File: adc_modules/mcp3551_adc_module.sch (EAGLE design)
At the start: 10 parts, among them U1 MCP3553-E/SN

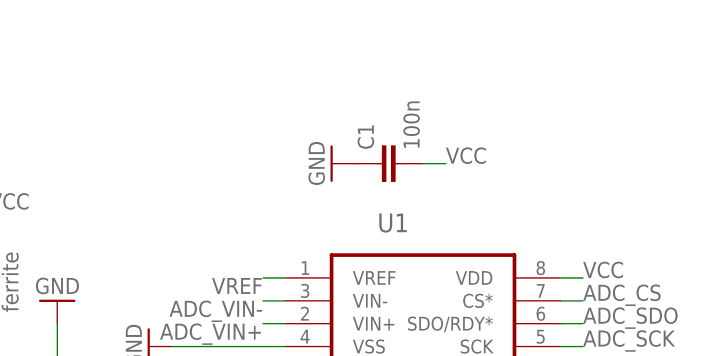
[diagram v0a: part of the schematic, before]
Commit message: * updated board format * made the LTC6655 reference module more compact, hopefully better * small modifications to the MCP355X ADC module
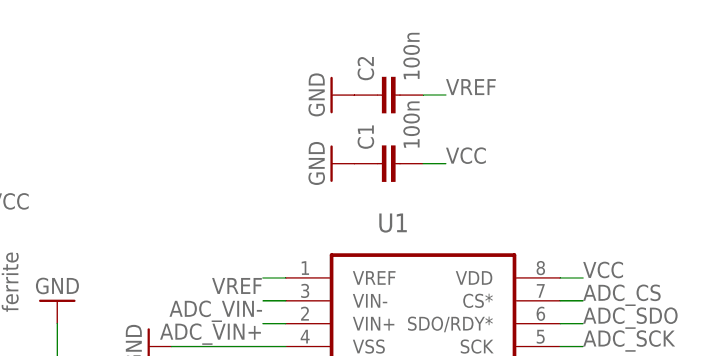
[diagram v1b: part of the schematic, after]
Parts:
- added C2: 100n, SquantorRCL:C-EUC0603
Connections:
- net GND: now also C2.1
- net VREF: now also C2.2
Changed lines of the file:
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@@
 <part name="R6" library="SquantorRCL" deviceset="R-EU_" device="R0805" value="5.1k"/>
 <part name="GND6" library="supply1" deviceset="GND" device=""/>
+<part name="C2" library="SquantorRCL" deviceset="C-EU" device="C0603" value="100n"/>
+<part name="GND7" library="supply1" deviceset="GND" device=""/>
 </parts>
 <sheets>
@@
 <instance part="R6" gate="G$1" x="17.78" y="7.62"/>
 <instance part="GND6" gate="1" x="22.86" y="0"/>
+<instance part="C2" gate="G$1" x="116.84" y="55.88" rot="R90"/>
+<instance part="GND7" gate="1" x="111.76" y="55.88" rot="R270"/>
 </instances>
 <busses>
@@
 <wire x1="22.86" y1="5.08" x2="25.4" y2="5.08" width="0.1524" layer="91"/>
 </segment>
+<segment>
+<pinref part="C2" gate="G$1" pin="1"/>
+<pinref part="GND7" gate="1" pin="GND"/>
+</segment>
 </net>
 <net name="N$1" class="0">
@@
 <junction x="22.86" y="17.78"/>
 </segment>
+<segment>
+<pinref part="C2" gate="G$1" pin="2"/>
+<wire x1="121.92" y1="55.88" x2="124.46" y2="55.88" width="0.1524" layer="91"/>
+<label x="124.46" y="55.88" size="1.778" layer="95"/>
+</segment>
 </net>
